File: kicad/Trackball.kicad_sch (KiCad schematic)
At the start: 49 parts, among them J1 Conn_01x04, J101 Conn_02x03_Counter_Clockwise, J2 Conn_02x04_Counter_Clockwise, SW1 Push_Button, SW101 Push_Button, SW102 Push_Button, SW103 Push_Button, SW104 Push_Button, SW106 Push_Button, SW2 Push_Button, SW3 RotaryEncoder_Switch_MP, U1 ESP32-S3-WROOM-1, U103 TCR2EF19, U2 PMW3360, U4 TLV73333PDBV

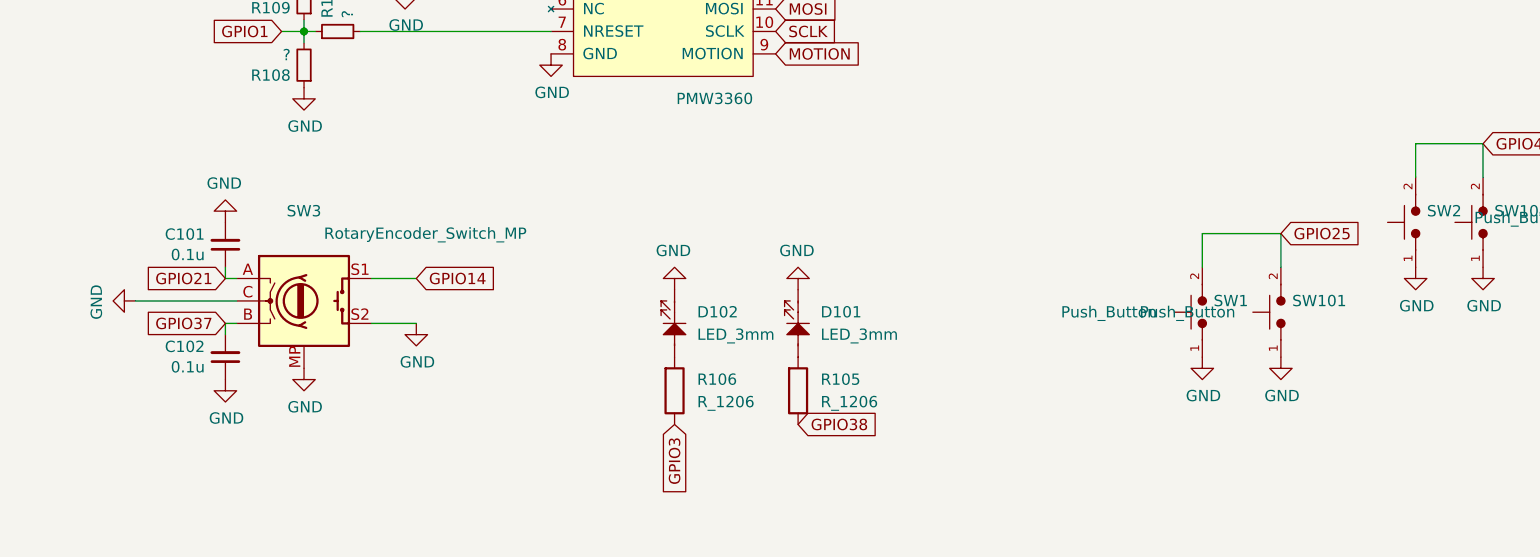
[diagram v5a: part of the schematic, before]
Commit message: re-asignement des pins gpio
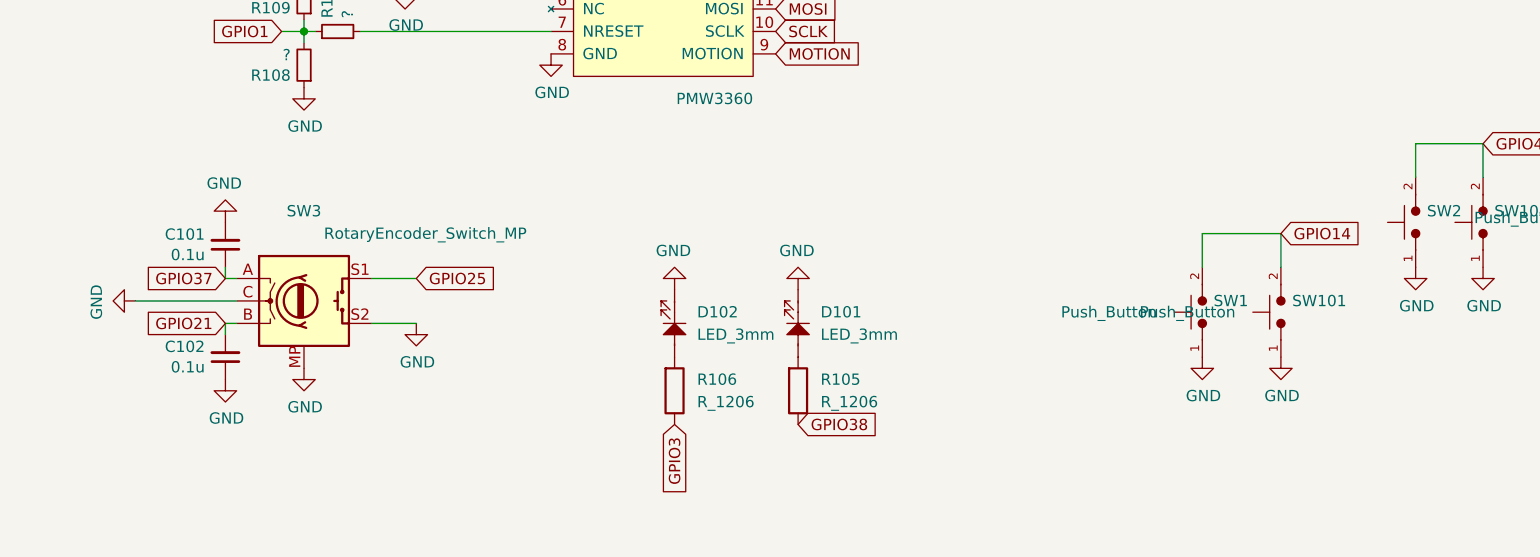
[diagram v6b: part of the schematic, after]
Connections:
- net GPIO14: now also SW1.2, SW101.2; no longer SW3.S1
- net GPIO21: now also C102.2, SW3.B; no longer C101.1, SW3.A
- net GPIO25: now also SW3.S1; no longer SW1.2, SW101.2
- net GPIO37: now also C101.1, SW3.A; no longer C102.2, SW3.B
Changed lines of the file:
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@@
 	(global_label "GPIO37"
 		(shape input)
-		(at 59.69 140.97 180)
+		(at 59.69 135.89 180)
 		(effects
 			(font
@@
 		)
 		(property "Intersheetrefs" "${INTERSHEET_REFS}"
-			(at 59.69 140.97 0)
+			(at 59.69 135.89 0)
 			(effects
 				(font
@@
 	(global_label "GPIO21"
 		(shape input)
-		(at 59.69 135.89 180)
+		(at 59.69 140.97 180)
 		(effects
 			(font
@@
 		)
 		(property "Intersheetrefs" "${INTERSHEET_REFS}"
-			(at 59.69 135.89 0)
+			(at 59.69 140.97 0)
 			(effects
 				(font
@@
 	(global_label "GPIO14"
 		(shape input)
-		(at 81.28 135.89 0)
-		(effects
-			(font
-				(size 1.27 1.27)
-			)
-			(justify left)
-		)
-		(property "Intersheetrefs" "${INTERSHEET_REFS}"
-			(at 81.28 135.89 0)
+		(at 179.07 130.81 0)
+		(effects
+			(font
+				(size 1.27 1.27)
+			)
+			(justify left)
+		)
+		(property "Intersheetrefs" "${INTERSHEET_REFS}"
+			(at 179.07 130.81 0)
 			(effects
 				(font
@@
 	(global_label "GPIO25"
 		(shape input)
-		(at 179.07 130.81 0)
-		(effects
-			(font
-				(size 1.27 1.27)
-			)
-			(justify left)
-		)
-		(property "Intersheetrefs" "${INTERSHEET_REFS}"
-			(at 179.07 130.81 0)
-			(effects
-				(font
+		(at 81.28 135.89 0)
+		(effects
+			(font
+				(size 1.27 1.27)
+			)
+			(justify left)
+		)
+		(property "Intersheetrefs" "${INTERSHEET_REFS}"
+			(at 81.28 135.89 0)
+			(effects
+				(font

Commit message: changement empreinte bouton en\gpio0
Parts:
- SW103, SW106: footprint Button_Switch_SMD:SW_Push_1P1T_NO_CK_KSC7xxJ -> Button_Switch_SMD:SW_SPST_CK_RS282G05A3
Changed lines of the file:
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@@
 			)
 		)
-		(property "Footprint" "Button_Switch_SMD:SW_Push_1P1T_NO_CK_KSC7xxJ"
+		(property "Footprint" "Button_Switch_SMD:SW_SPST_CK_RS282G05A3"
 			(at 299.085 35.687 0)
 			(effects
@@
 			)
 		)
-		(property "Footprint" "Button_Switch_SMD:SW_Push_1P1T_NO_CK_KSC7xxJ"
+		(property "Footprint" "Button_Switch_SMD:SW_SPST_CK_RS282G05A3"
 			(at 167.005 24.257 0)
 			(effects
